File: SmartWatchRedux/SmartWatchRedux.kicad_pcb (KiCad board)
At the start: 2 copper layers, 20.3 x 65.1 mm, 6 parts, among them CN1 27C256Socket, U1 ROM, U2 DS1315, Y1 32.768 KHz

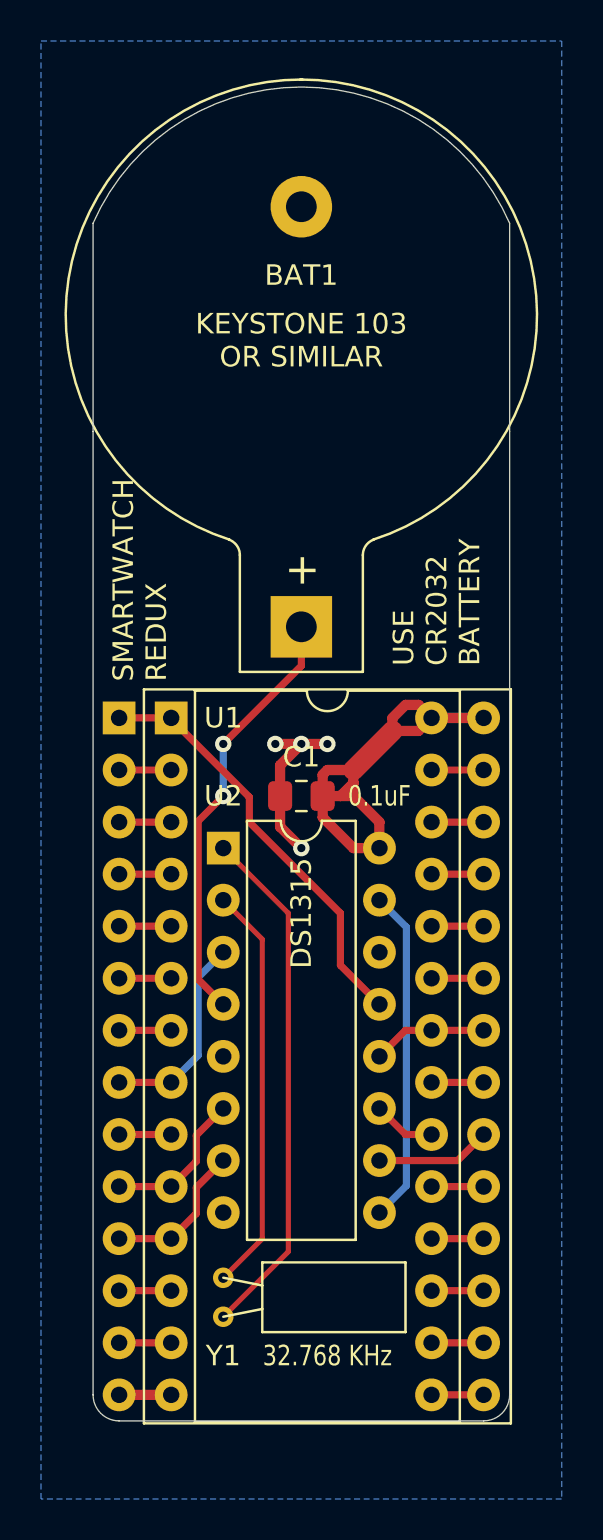
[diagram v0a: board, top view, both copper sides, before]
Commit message: Relocate crystal to be above DS1315 and closer to X1/X2 pins
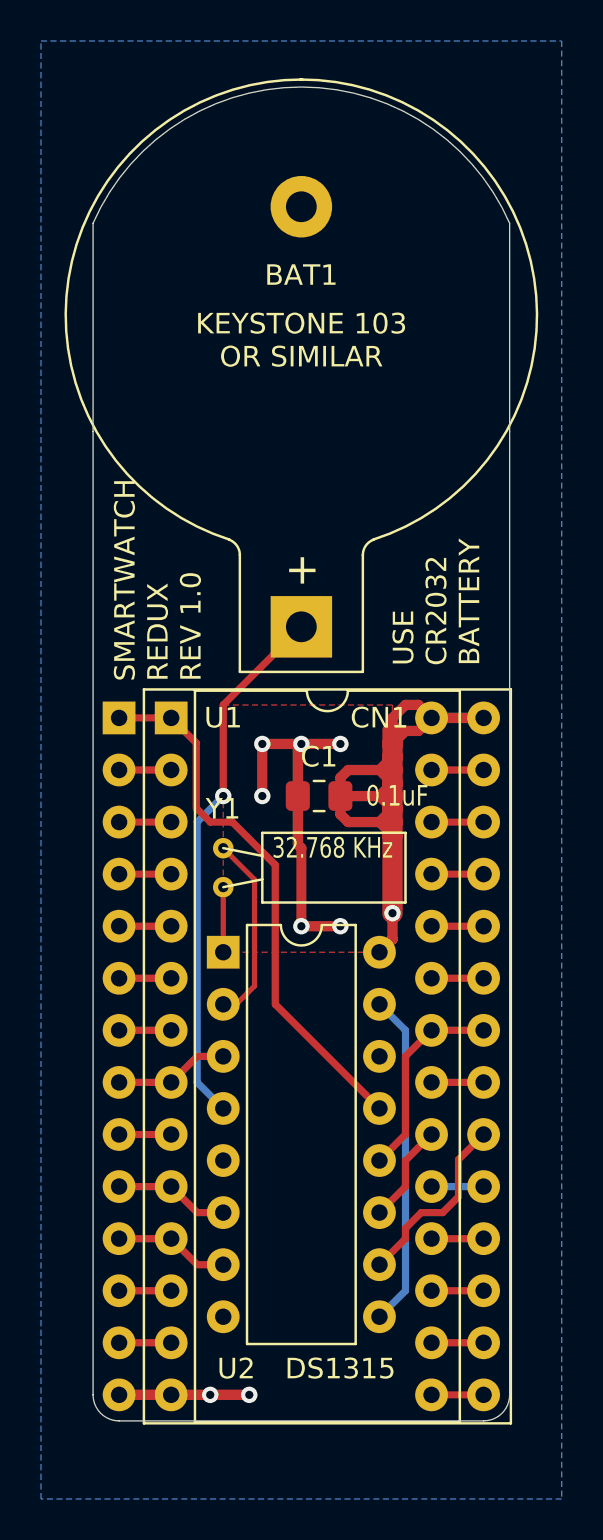
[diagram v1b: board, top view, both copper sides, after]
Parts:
- moved Y1 21.0 mm to (113.0, 71.8)
- moved U2 5.08 mm to (113.0, 74.9)
- moved C1 0.87 mm to (117.7, 67.3)
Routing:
- net /XTAL1: track 25.5 -> 3.18 mm
- net GND: track 11.0 -> 23.6 mm, vias 4 -> 8
- net VCC: track 27.4 -> 39.5 mm, vias 0 -> 1
- net /XTAL2: track 20.0 -> 9.25 mm
- net Net-(CN1-Pad1): track 20.7 -> 26.4 mm
- net Net-(BAT1-Pad1): track 21.0 -> 26.1 mm, vias 2 -> 1
- net Net-(CN1-Pad8): track 9.94 -> 5.61 mm
- net Net-(CN1-Pad22): track 5.61 -> 9.94 mm
- net Net-(U1-Pad20): track 5.61 -> 9.06 mm
- net Net-(CN1-Pad11): track 7.40 -> 5.61 mm
- net Net-(CN1-Pad10): track 7.40 -> 5.61 mm
- net Net-(CN1-Pad20): track 3.07 -> 4.86 mm
- added copper zone on F.Cu, net GND
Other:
- board text added: "SMARTWATCH REDUX REV 1.0"
- board text removed: "SMARTWATCH REDUX"
